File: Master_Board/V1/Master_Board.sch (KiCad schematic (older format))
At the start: 8 parts, among them J101 Header_Male_Pin_2.54mm_1X2_,_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, J102 Header_Male_Pin_2.54mm_1X2_,_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, J103 Header_Male_Pin_2.54mm_1X2_,_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, J104 Header_Male_Pin_2.54mm_1X2_,_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, J105 Header_Male_Pin_2.54mm_1X2_,_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, J106 Header_Male_Pin_2.54mm_1X2_,_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, J107 Header_Male_Pin_2.54mm_1X38_,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, J108 Header_Male_Pin_2.54mm_1X3_,_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

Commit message: Add Master_Board modules
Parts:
- removed J107: Header_Male_Pin_2.54mm_1X38_,_Unshrouded, Connectors:Headers_2.54mm_1X38, symbol Header_Male_Pin_2.54mm_1X38_,_Unshrouded
- added J?: 649022227222, Connectors:649022227222, symbol 649022227222
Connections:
- net labels added: 12V_IN, ANA1, ANA2, ANA_IN, ANA_SUP, CAN2_H, CAN2_L, GND, IO1, IO2, IO3, IO4, IO5, IO6, IO7, IO8, PWM2_OUT, PWM_COM, RS232_RX, RX232_RX, RX232_TX, RXD, TXD
- wire segments 99 -> 101
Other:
- moved on the sheet: J108

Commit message: git modify Master_board
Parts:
- removed J101, J102, J103, J104, J105, J106: Header_Male_Pin_2.54mm_1X2_,_Unshrouded, Connectors:Headers_2.54mm_1X2, symbol Header_Male_Pin_2.54mm_1X2_,_Unshrouded
- gave numbers to parts that had none: 1
- renumbered J108 to J102
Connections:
- net PA12: no longer J101.14
- net RS232_RX renamed PA2
- new net PA3: J101.14
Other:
- moved on the sheet: J101

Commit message: Add page LedDriver
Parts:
- removed J102: Header_Male_Pin_2.54mm_1X3_,_Unshrouded, Connectors:Headers_2.54mm_1X3, symbol Header_Male_Pin_2.54mm_1X3_,_Unshrouded
- added F? (x2): 39511000440, Fuses:TE5_395, symbol 39511000440
- added Q102, Q? (x2): BSS806NH6327XTSA1, IC:SOT-23-3, symbol BSS806NH6327XTSA1
- added Q103: 2N7002P,215, IC:SOT-23-3, symbol 2N7002P,215
- added R101, R102, R? (x2): RC0805JR-07100KL, Resistors:R0805, symbol RC0805JR-07100KL
- added R?: RC0805JR-076K8L, Resistors:R0805, symbol RC0805JR-076K8L
- added U? (x2): LMV321RILT, IC:SOT-23-5, symbol LMV321RILT
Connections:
- net labels added: 12V_IN1, 12V_IN2, 3.3V, CAN1_RX, CAN1_TX, CAN2_RX, CAN2_TX, MainContactor+, MainContactor-, MpptContactor, NTC_1_ADC, NTC_1_GPIO, USART2_RX, USART2_TX
- net labels removed: 12V_IN
- wire segments 73 -> 138
- no-connect marks 0 -> 1
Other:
- note added: "DAC Protection"
- note added: "External PWM"
- note added: "GPIO"
- moved on the sheet: J101

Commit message: Modify MasterBoard.sch
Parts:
- removed R?: RC0805JR-076K8L, Resistors:R0805, symbol RC0805JR-076K8L
- added R?: RC0805JR-07330RL, Resistors:R0805, symbol RC0805JR-07330RL
- added R? (x3): RC0805JR-07100RL, Resistors:R0805, symbol RC0805JR-07100RL
- added U?: LMV321RILT, IC:SOT-23-5, symbol LMV321RILT
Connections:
- wire segments 138 -> 165
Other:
- note added: "Analog Protection"
- note removed: "DAC Protection"
- moved on the sheet: F?, Q103, Q?, R102, R?, U?

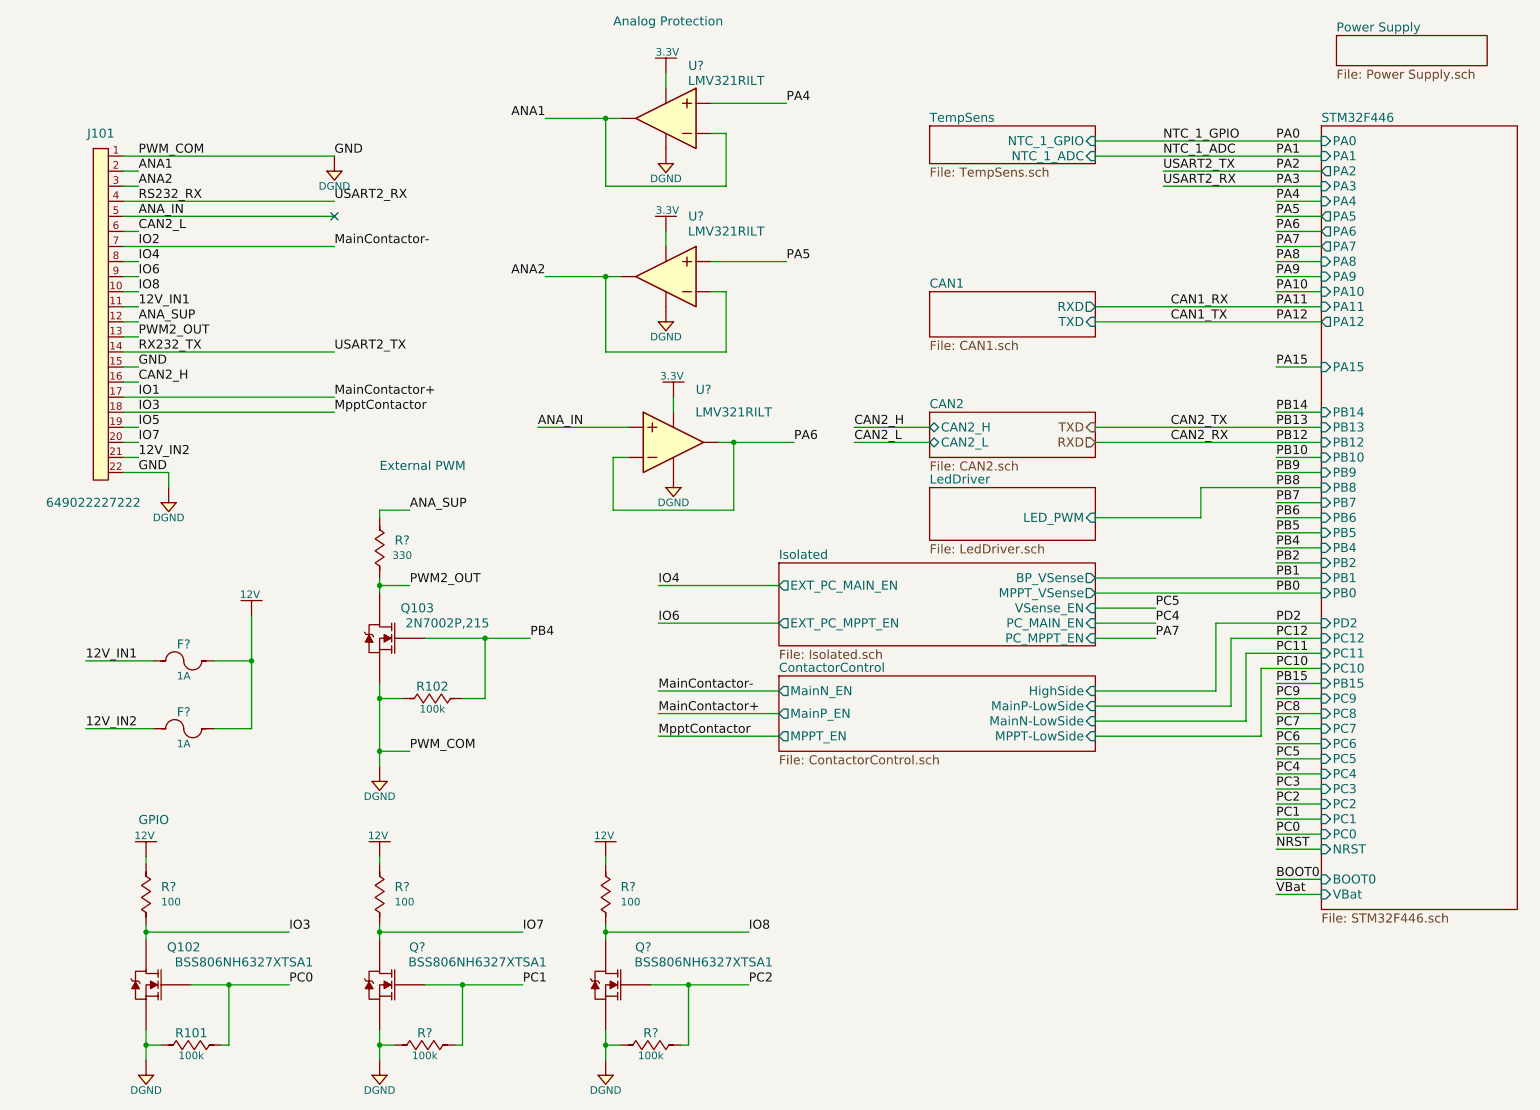
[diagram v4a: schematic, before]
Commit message: Add page LEDDriver.sch
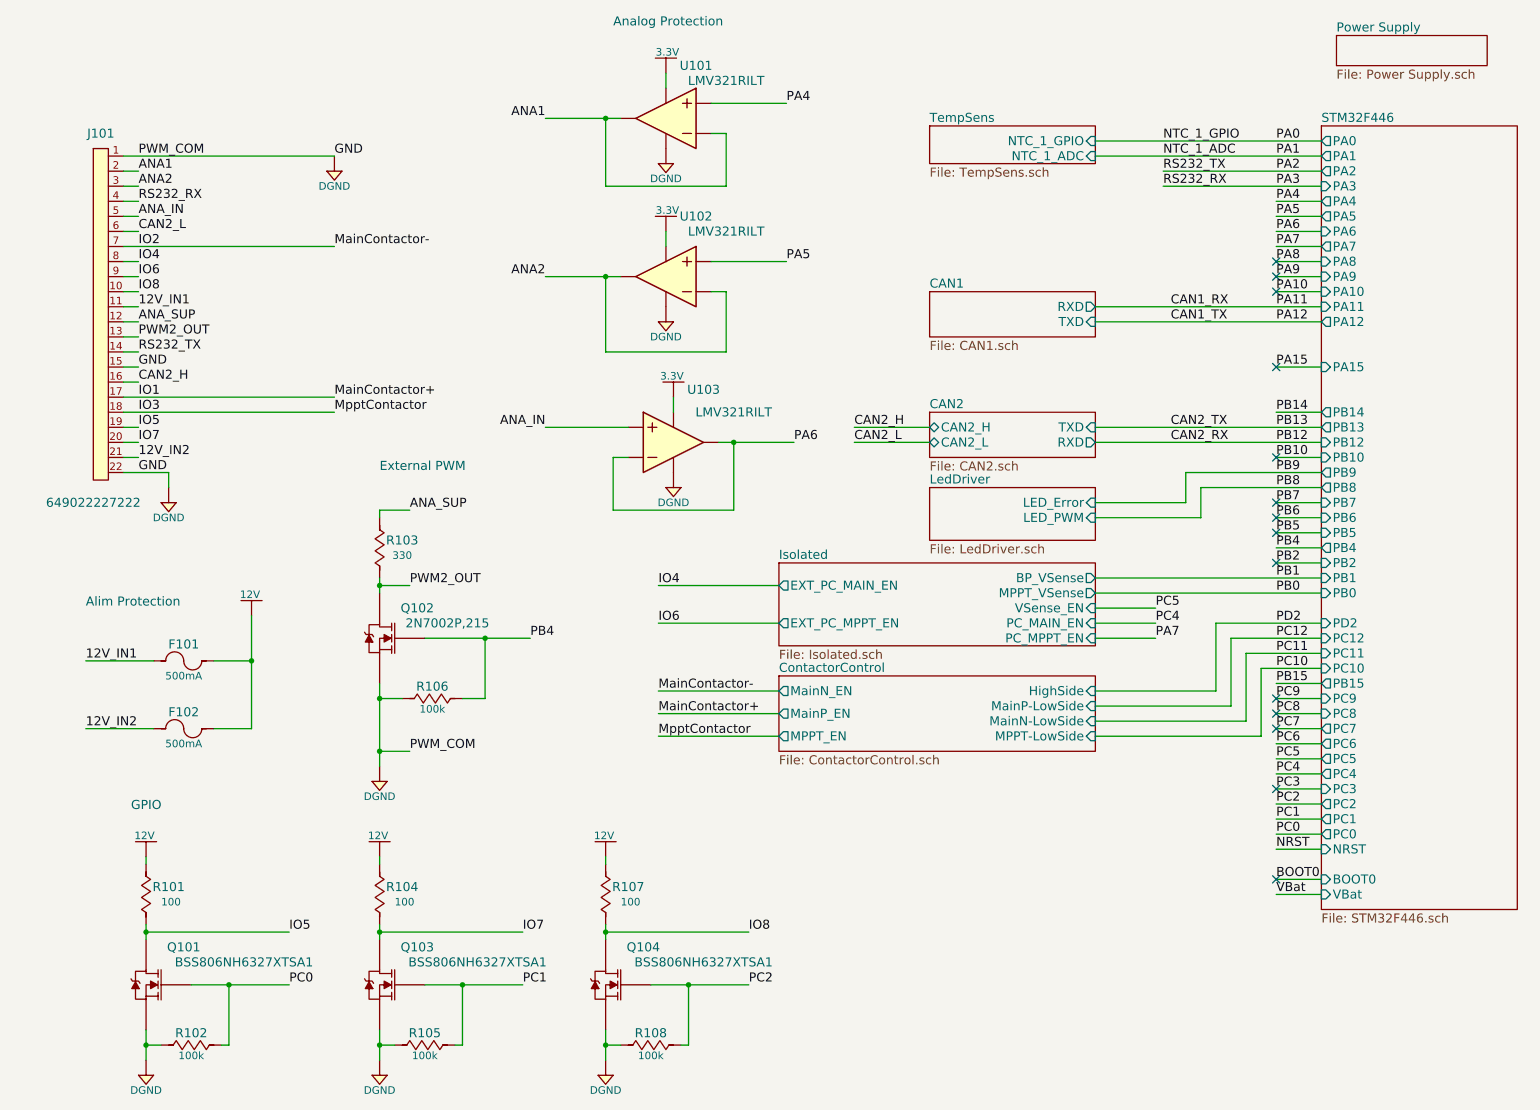
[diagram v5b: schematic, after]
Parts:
- removed F? (x2): 39511000440, Fuses:TE5_395, symbol 39511000440
- added F101, F102: 39505000440, Fuses:TE5_395, symbol 39505000440
- gave numbers to parts that had none: 11
- renumbered Q102 to Q101, Q103 to Q102, R101 to R102, R102 to R106
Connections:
- net 12V: now also F101.2, F102.2
- net 12V_IN1: now also F101.1
- net 12V_IN2: now also F102.1
- net IO3: no longer Q101.3 (D), R101.2
- net IO5: now also Q101.3 (D), R101.2
- no-connect marks 1 -> 14
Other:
- note added: "Alim Protection"

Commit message: Release1 MasterBoard PCB
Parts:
- removed U103: LMV321RILT, IC:SOT-23-5, symbol LMV321RILT
- added C101: 885012207092, Capacitors:C0805, symbol 885012207092
- added D101, D102: SD0805S020S1R0, Diodes:Diode_0805, symbol SD0805S020S1R0
- added R109: RC0805JR-072KL, Resistors:R0805, symbol RC0805JR-072KL
- added R110: RC0805JR-07680RL, Resistors:R0805, symbol RC0805JR-07680RL
- added R111: RC0805JR-0710RL, Resistors:R0805, symbol RC0805JR-0710RL
- added R112: RC0805JR-071KL, Resistors:R0805, symbol RC0805JR-071KL
- added R113: RC0805JR-07100KL, Resistors:R0805, symbol RC0805JR-07100KL
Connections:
- net 3.3V: now also D101.1 (Cathode), R113.1
- net ANA_IN: now also R109.1
- net DGND: now also C101.2, D102.2 (Anode), R110.2
- net PA6: now also C101.1, R112.2, R113.2
- new net: R109.2, R110.1, R111.1
- new net: D101.2 (Anode), D102.1 (Cathode), R111.2, R112.1
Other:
- moved on the sheet: U101, U102

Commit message: Fix some routing on MasterBoard
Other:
- note added: "12V"
- note added: "3.045V"
- note added: "Analog Input"
- note added: "Digital-to-Analog Converter"
- note removed: "Analog Protection"
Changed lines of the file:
@@
 EESchema Schematic File Version 2
-LIBS:Master_Board-rescue
+LIBS:ADC
 LIBS:Amplifiers
+LIBS:Battery
 LIBS:Capacitors
+LIBS:Comparators
 LIBS:Connectors
+LIBS:Crystals
+LIBS:DAC
 LIBS:Diodes
 LIBS:Fuses
 LIBS:Inductors
+LIBS:Interface
+LIBS:Isolators
+LIBS:STMicroelectronics
 LIBS:PMIC
+LIBS:Power_Port
 LIBS:Relays
 LIBS:Resistors
 LIBS:Sensors
+LIBS:Switches
+LIBS:Transformers
+LIBS:Transistors
 LIBS:Master_Board-cache
 EELAYER 25 0
@@
 	1900 5300 1650 5300
 Connection ~ 1900 4850
-Text Notes 4200 750  0    60   ~ 0
-Analog Protection
+Text Notes 3950 650  0    60   ~ 0
+Digital-to-Analog Converter
 Text Notes 1100 5850 0    60   ~ 0
 GPIO
@@
 Wire Wire Line
 	3000 1650 3800 1650
+Text Notes 5400 2650 0    60   ~ 0
+3.045V
+Text Notes 3400 2700 0    60   ~ 0
+12V
+Text Notes 3800 2100 0    60   ~ 0
+Analog Input
 $EndSCHEMATC
